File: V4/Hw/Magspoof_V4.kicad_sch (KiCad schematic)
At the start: 35 parts, among them J1 Coil, J2 SWD, P1 USB_C_Plug_USB2.0, Q1 DMG3415U-7, SW1 ON, SW3 S1, SW4 SOURCE MAG, SW5 RESET, U1 CH552G, U2 AP2112K-3.3, U3 TC4424, U5 MCP73831

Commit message: add lcsc components to BOM
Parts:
- C1, C2: LCSC# (none) -> C2171572; Proveedor MOUSER -> LCSC
- C17, C18, C3, C4: LCSC# C2992625 -> C315248; manf# 0402X106M100CT -> CL05A106MP5NUNC
- D3: LCSC# (none) -> C205442; Proveedor MOUSER -> LCSC
- D4: LCSC# (none) -> C130114
- F1: LCSC# (none) -> C2649565
- R1: LCSC# (none) -> C2759509
- R10: LCSC# (none) -> C114877
- R11: LCSC# (none) -> C192169
- R7: LCSC# (none) -> C138045
- SW1: LCSC# - -> C221660; Proveedor (none) -> LCSC
- SW4: LCSC# (none) -> C221660; Proveedor MOUSER -> LCSC
- U3: LCSC# (none) -> C636876; Proveedor (none) -> MOUSER
- U5: LCSC# (none) -> C38066
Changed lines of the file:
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@@
       (effects (font (size 1.27 1.27)) hide)
     )
-    (property "LCSC#" "" (at 216.789 77.216 0)
+    (property "LCSC#" "C636876" (at 216.789 77.216 0)
+      (effects (font (size 1.27 1.27)) hide)
+    )
+    (property "Proveedor" "MOUSER" (at 216.789 77.216 0)
       (effects (font (size 1.27 1.27)) hide)
     )
@@
       (effects (font (size 1.27 1.27)) hide)
     )
+    (property "LCSC#" "C38066" (at 228.854 27.686 0)
+      (effects (font (size 1.27 1.27)) hide)
+    )
     (pin "1")
     (pin "2")
@@
       (effects (font (size 1.27 1.27)) hide)
     )
-    (property "manf#" "0402X106M100CT" (at 118.872 39.497 0)
-      (effects (font (size 1.27 1.27)) hide)
-    )
-    (property "LCSC#" "C2992625" (at 118.872 39.497 0)
+    (property "manf#" "CL05A106MP5NUNC" (at 118.872 39.497 0)
+      (effects (font (size 1.27 1.27)) hide)
+    )
+    (property "LCSC#" "C315248" (at 118.872 39.497 0)
       (effects (font (size 1.27 1.27)) hide)
     )
@@
       (effects (font (size 1.27 1.27)) hide)
     )
-    (property "LCSC#" "" (at 107.061 107.442 0)
+    (property "LCSC#" "C2759509" (at 107.061 107.442 0)
       (effects (font (size 1.27 1.27)) hide)
     )
@@
       (effects (font (size 1.27 1.27)) hide)
     )
-    (property "LCSC#" "" (at 147.32 43.053 0)
+    (property "LCSC#" "C138045" (at 147.32 43.053 0)
       (effects (font (size 1.27 1.27)) hide)
     )
@@
       (effects (font (size 1.27 1.27)) hide)
     )
-    (property "LCSC#" "" (at 53.34 106.68 0)
-      (effects (font (size 1.27 1.27)) hide)
-    )
-    (property "Proveedor" "MOUSER" (at 53.34 106.68 0)
+    (property "LCSC#" "C2171572" (at 53.34 106.68 0)
+      (effects (font (size 1.27 1.27)) hide)
+    )
+    (property "Proveedor" "LCSC" (at 53.34 106.68 0)
       (effects (font (size 1.27 1.27)) hide)
     )
@@
       (effects (font (size 1.27 1.27)) hide)
     )
-    (property "manf#" "0402X106M100CT" (at 201.295 36.576 0)
-      (effects (font (size 1.27 1.27)) hide)
-    )
-    (property "LCSC#" "C2992625" (at 201.295 36.576 0)
+    (property "manf#" "CL05A106MP5NUNC" (at 201.295 36.576 0)
+      (effects (font (size 1.27 1.27)) hide)
+    )
+    (property "LCSC#" "C315248" (at 201.295 36.576 0)
       (effects (font (size 1.27 1.27)) hide)
     )
@@
       (effects (font (size 1.27 1.27)) hide)
     )
+    (property "LCSC#" "C114877" (at 243.713 35.687 0)
+      (effects (font (size 1.27 1.27)) hide)
+    )
     (pin "1")
     (pin "2")
@@
       (effects (font (size 1.27 1.27)) hide)
     )
-    (property "LCSC#" "-" (at 85.725 36.957 0)
+    (property "LCSC#" "C221660" (at 85.725 36.957 0)
       (effects (font (size 1.27 1.27)) hide)
     )
     (property "manf#" "JS102011SAQN" (at 85.725 36.957 0)
+      (effects (font (size 1.27 1.27)) hide)
+    )
+    (property "Proveedor" "LCSC" (at 85.725 36.957 0)
       (effects (font (size 1.27 1.27)) hide)
     )
@@
       (effects (font (size 1.27 1.27)) hide)
     )
+    (property "LCSC#" "C130114" (at 243.713 44.45 0)
+      (effects (font (size 1.27 1.27)) hide)
+    )
     (pin "1")
     (pin "2")
@@
       (effects (font (size 1.27 1.27)) hide)
     )
-    (property "Proveedor" "MOUSER" (at 147.32 32.512 0)
+    (property "Proveedor" "LCSC" (at 147.32 32.512 0)
+      (effects (font (size 1.27 1.27)) hide)
+    )
+    (property "LCSC#" "C205442" (at 147.32 32.512 0)
       (effects (font (size 1.27 1.27)) hide)
     )
@@
       (effects (font (size 1.27 1.27)) hide)
     )
-    (property "manf#" "0402X106M100CT" (at 94.488 41.529 0)
-      (effects (font (size 1.27 1.27)) hide)
-    )
-    (property "LCSC#" "C2992625" (at 94.488 41.529 0)
+    (property "manf#" "CL05A106MP5NUNC" (at 94.488 41.529 0)
+      (effects (font (size 1.27 1.27)) hide)
+    )
+    (property "LCSC#" "C315248" (at 94.488 41.529 0)
       (effects (font (size 1.27 1.27)) hide)
     )
@@
       (effects (font (size 1.27 1.27)) hide)
     )
-    (property "LCSC#" "" (at 65.532 43.688 0)
+    (property "LCSC#" "C192169" (at 65.532 43.688 0)
       (effects (font (size 1.27 1.27)) hide)
     )
@@
       (effects (font (size 1.27 1.27)) hide)
     )
-    (property "manf#" "0402X106M100CT" (at 262.001 36.703 0)
-      (effects (font (size 1.27 1.27)) hide)
-    )
-    (property "LCSC#" "C2992625" (at 262.001 36.703 0)
+    (property "manf#" "CL05A106MP5NUNC" (at 262.001 36.703 0)
+      (effects (font (size 1.27 1.27)) hide)
+    )
+    (property "LCSC#" "C315248" (at 262.001 36.703 0)
       (effects (font (size 1.27 1.27)) hide)
     )
@@
       (effects (font (size 1.27 1.27)) hide)
     )
-    (property "Proveedor" "MOUSER" (at 239.649 73.406 0)
+    (property "Proveedor" "LCSC" (at 239.649 73.406 0)
+      (effects (font (size 1.27 1.27)) hide)
+    )
+    (property "LCSC#" "C221660" (at 239.649 73.406 0)
       (effects (font (size 1.27 1.27)) hide)
     )
@@
       (effects (font (size 1.27 1.27)) hide)
     )
-    (property "LCSC#" "" (at 58.801 100.33 0)
-      (effects (font (size 1.27 1.27)) hide)
-    )
-    (property "Proveedor" "MOUSER" (at 58.801 100.33 0)
+    (property "LCSC#" "C2171572" (at 58.801 100.33 0)
+      (effects (font (size 1.27 1.27)) hide)
+    )
+    (property "Proveedor" "LCSC" (at 58.801 100.33 0)
       (effects (font (size 1.27 1.27)) hide)
     )
@@
       (effects (font (size 1.27 1.27)) hide)
     )
+    (property "LCSC#" "C2649565" (at 45.339 30.48 0)
+      (effects (font (size 1.27 1.27)) hide)
+    )

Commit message: Change components for JLCPCB
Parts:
- F1: footprint Fuse:Fuse_0805_2012Metric -> Fuse:Fuse_0603_1608Metric; LCSC# C2649565 -> C136327; Proveedor MOUSER -> LCSC; manf# MFU0805FF00500P100 -> (none)
- SW1, SW4: footprint Library:JS102011SAQN -> Library:SW-SMD_K3-1280S-K1; LCSC# C221660 -> C92658; manf# JS102011SAQN -> (none)
- U3: LCSC# C636876 -> C44150; manf# TC4424AVOA -> TC4424AVOA713
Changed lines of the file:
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@@
       (effects (font (size 1.524 1.524)) hide)
     )
-    (property "manf#" "TC4424AVOA" (at 216.789 77.216 0)
-      (effects (font (size 1.27 1.27)) hide)
-    )
-    (property "LCSC#" "C636876" (at 216.789 77.216 0)
+    (property "manf#" "TC4424AVOA713" (at 216.789 77.216 0)
+      (effects (font (size 1.27 1.27)) hide)
+    )
+    (property "LCSC#" "C44150" (at 216.789 77.216 0)
       (effects (font (size 1.27 1.27)) hide)
     )
@@
       (effects (font (size 1.27 1.27)))
     )
-    (property "Footprint" "Library:JS102011SAQN" (at 85.725 36.957 0)
+    (property "Footprint" "Library:SW-SMD_K3-1280S-K1" (at 85.725 36.957 0)
       (effects (font (size 1.27 1.27)) hide)
     )
@@
       (effects (font (size 1.27 1.27)) hide)
     )
-    (property "LCSC#" "C221660" (at 85.725 36.957 0)
-      (effects (font (size 1.27 1.27)) hide)
-    )
-    (property "manf#" "JS102011SAQN" (at 85.725 36.957 0)
+    (property "LCSC#" "C92658" (at 85.725 36.957 0)
+      (effects (font (size 1.27 1.27)) hide)
+    )
+    (property "manf#" "" (at 85.725 36.957 0)
       (effects (font (size 1.27 1.27)) hide)
     )
@@
       (effects (font (size 1.27 1.27)) (justify left))
     )
-    (property "Footprint" "Library:JS102011SAQN" (at 239.649 73.406 0)
+    (property "Footprint" "Library:SW-SMD_K3-1280S-K1" (at 239.649 73.406 0)
       (effects (font (size 1.27 1.27)) hide)
     )
@@
       (effects (font (size 1.27 1.27)) hide)
     )
-    (property "manf#" "JS102011SAQN" (at 239.649 73.406 0)
+    (property "manf#" "" (at 239.649 73.406 0)
       (effects (font (size 1.27 1.27)) hide)
     )
@@
       (effects (font (size 1.27 1.27)) hide)
     )
-    (property "LCSC#" "C221660" (at 239.649 73.406 0)
+    (property "LCSC#" "C92658" (at 239.649 73.406 0)
+      (effects (font (size 1.27 1.27)) hide)
+    )
+    (property "Campo7" "" (at 239.649 73.406 90)
       (effects (font (size 1.27 1.27)) hide)
     )
@@
       (effects (font (size 1.27 1.27)))
     )
-    (property "Footprint" "Fuse:Fuse_0805_2012Metric" (at 45.339 30.48 0)
+    (property "Footprint" "Fuse:Fuse_0603_1608Metric" (at 45.339 30.48 0)
       (effects (font (size 1.27 1.27)) hide)
     )
@@
       (effects (font (size 1.27 1.27)) hide)
     )
-    (property "manf#" "MFU0805FF00500P100" (at 45.339 30.48 0)
-      (effects (font (size 1.27 1.27)) hide)
-    )
-    (property "Proveedor" "MOUSER" (at 45.339 30.48 0)
-      (effects (font (size 1.27 1.27)) hide)
-    )
-    (property "LCSC#" "C2649565" (at 45.339 30.48 0)
-      (effects (font (size 1.27 1.27)) hide)
-    )
+    (property "manf#" "" (at 45.339 30.48 0)
+      (effects (font (size 1.27 1.27)) hide)
+    )
+    (property "Proveedor" "LCSC" (at 45.339 30.48 0)
+      (effects (font (size 1.27 1.27)) hide)
+    )
+    (property "LCSC#" "C136327" (at 45.339 30.48 0)
+      (effects (font (size 1.27 1.27)) hide)
+    )

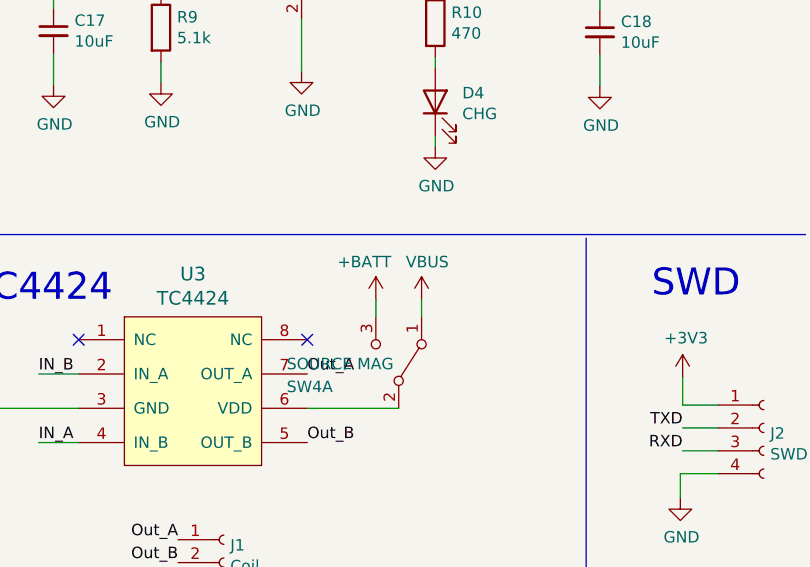
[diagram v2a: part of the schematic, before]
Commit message: change footprint of SW1,4, and F1 and routing
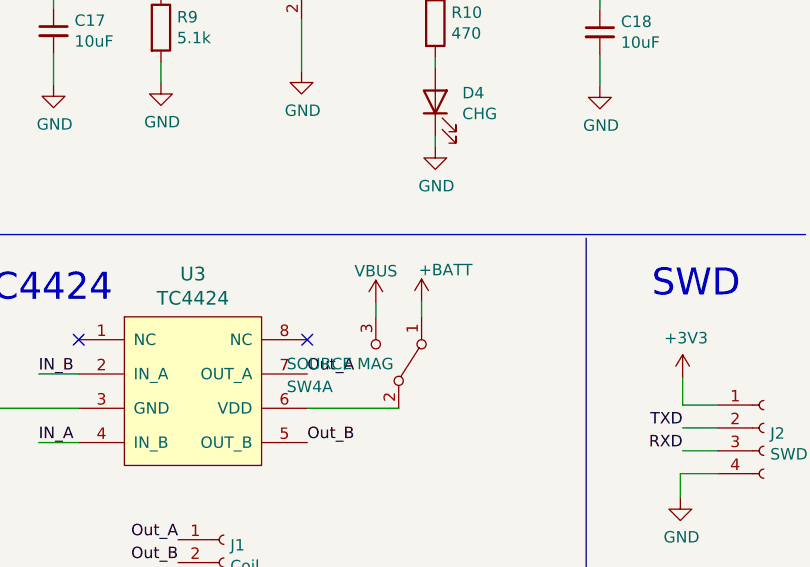
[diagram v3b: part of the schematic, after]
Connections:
- net +BATT: now also SW4.1 (A); no longer SW4.3 (C)
- net VBUS: now also SW4.3 (C); no longer SW4.1 (A)
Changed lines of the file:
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@@
-    (stroke (width 0) (type default))
-  )
-  (wire (pts (xy 237.109 68.326) (xy 237.109 66.421))
     (stroke (width 0) (type default))
   )
@@
     (stroke (width 0) (type default))
   )
+  (wire (pts (xy 242.189 66.675) (xy 242.189 68.326))
+    (stroke (width 0) (type default))
+  )
   (wire (pts (xy 79.121 105.41) (xy 82.169 105.41))
     (stroke (width 0) (type default))
@@
     (stroke (width 0) (type default))
   )
+  (wire (pts (xy 237.109 66.802) (xy 237.109 68.326))
+    (stroke (width 0) (type default))
+  )
   (wire (pts (xy 40.386 35.56) (xy 41.783 35.56))
     (stroke (width 0) (type default))
   )
   (wire (pts (xy 94.488 38.989) (xy 94.488 36.957))
-    (stroke (width 0) (type default))
-  )
-  (wire (pts (xy 242.189 68.326) (xy 242.189 66.421))
     (stroke (width 0) (type default))
   )
@@
     )
   )
-  (symbol (lib_id "power:+BATT") (at 237.109 66.421 0) (unit 1)
-    (in_bom yes) (on_board yes) (dnp no)
-    (property "Reference" "#PWR057" (at 237.109 70.231 0)
-      (effects (font (size 1.27 1.27)) hide)
-    )
-    (property "Value" "+BATT" (at 235.839 62.23 0)
-      (effects (font (size 1.27 1.27)))
-    )
-    (property "Footprint" "" (at 237.109 66.421 0)
-      (effects (font (size 1.27 1.27)) hide)
-    )
-    (property "Datasheet" "" (at 237.109 66.421 0)
+  (symbol (lib_id "power:+BATT") (at 242.189 66.675 0) (unit 1)
+    (in_bom yes) (on_board yes) (dnp no)
+    (property "Reference" "#PWR057" (at 242.189 70.485 0)
+      (effects (font (size 1.27 1.27)) hide)
+    )
+    (property "Value" "+BATT" (at 244.856 63.119 0)
+      (effects (font (size 1.27 1.27)))
+    )
+    (property "Footprint" "" (at 242.189 66.675 0)
+      (effects (font (size 1.27 1.27)) hide)
+    )
+    (property "Datasheet" "" (at 242.189 66.675 0)
       (effects (font (size 1.27 1.27)) hide)
     )
@@
     )
   )
-  (symbol (lib_id "power:VBUS") (at 242.189 66.421 0) (unit 1)
-    (in_bom yes) (on_board yes) (dnp no)
-    (property "Reference" "#PWR058" (at 242.189 70.231 0)
-      (effects (font (size 1.27 1.27)) hide)
-    )
-    (property "Value" "VBUS" (at 242.824 62.23 0)
-      (effects (font (size 1.27 1.27)))
-    )
-    (property "Footprint" "" (at 242.189 66.421 0)
-      (effects (font (size 1.27 1.27)) hide)
-    )
-    (property "Datasheet" "" (at 242.189 66.421 0)
-      (effects (font (size 1.27 1.27)) hide)
-    )
+  (symbol (lib_id "power:VBUS") (at 237.109 66.802 0) (unit 1)
+    (in_bom yes) (on_board yes) (dnp no)
+    (property "Reference" "#PWR058" (at 237.109 70.612 0)
+      (effects (font (size 1.27 1.27)) hide)
+    )
+    (property "Value" "VBUS" (at 237.109 63.246 0)
+      (effects (font (size 1.27 1.27)))
+    )
+    (property "Footprint" "" (at 237.109 66.802 0)
+      (effects (font (size 1.27 1.27)) hide)
+    )
+    (property "Datasheet" "" (at 237.109 66.802 0)
+      (effects (font (size 1.27 1.27)) hide)
+    )

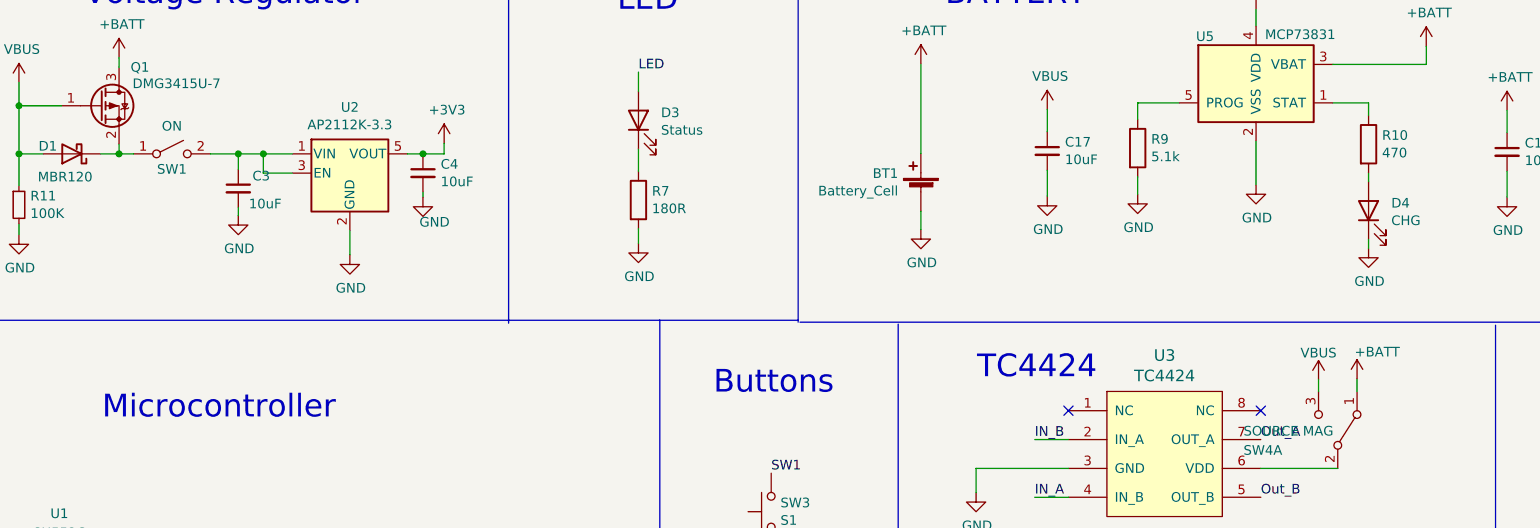
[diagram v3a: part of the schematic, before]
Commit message: change SW1 and SW4 for stocks
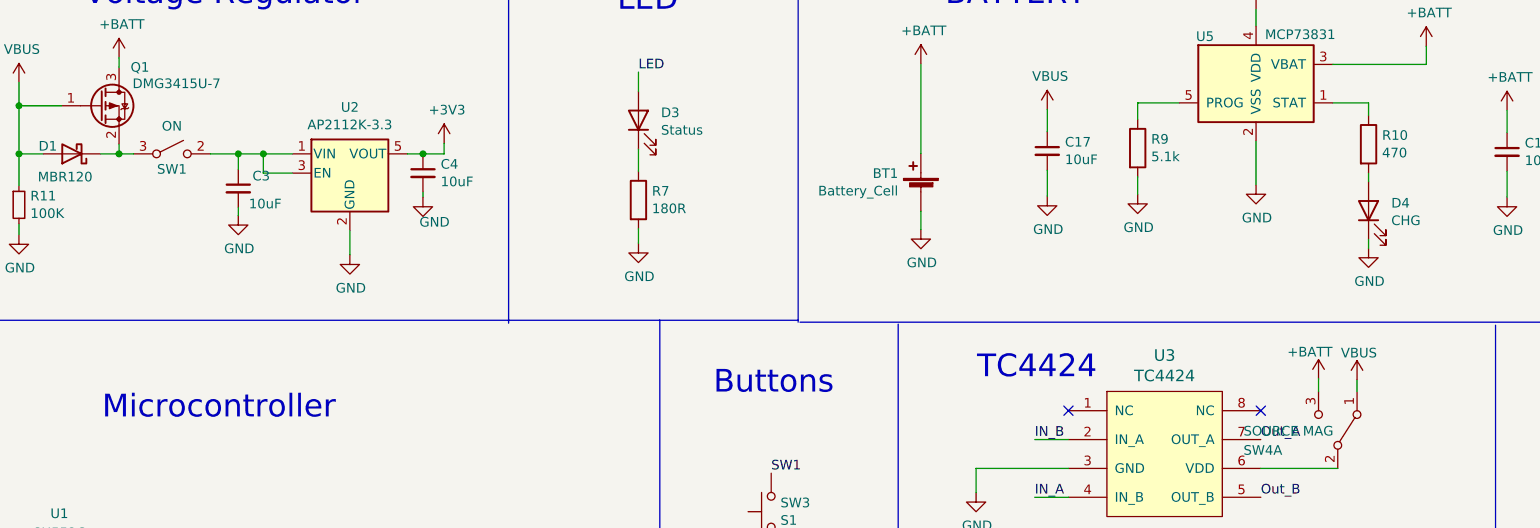
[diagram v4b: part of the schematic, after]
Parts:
- SW1, SW4: footprint Library:SW-SMD_K3-1280S-K1 -> Library:SW-SMD_SSSS811101; LCSC# C92658 -> C109335
- SW3, SW5: LCSC# C2886897 -> C318889
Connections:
- net +BATT: now also SW4.3 (C); no longer SW4.1 (A)
- net VBUS: now also SW4.1 (A); no longer SW4.3 (C)
- net at D1.1 (K), Q1.2 (S): now also SW1.3 (A); no longer SW1.1 (A)
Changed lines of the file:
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@@
-    (stroke (width 0) (type default))
-  )
-  (wire (pts (xy 242.189 66.675) (xy 242.189 68.326))
     (stroke (width 0) (type default))
   )
@@
     (stroke (width 0) (type default))
   )
+  (wire (pts (xy 237.109 66.675) (xy 237.109 68.326))
+    (stroke (width 0) (type default))
+  )
   (wire (pts (xy 271.1958 78.1304) (xy 271.1958 75.0824))
     (stroke (width 0) (type default))
@@
     (stroke (width 0) (type default))
   )
-  (wire (pts (xy 237.109 66.802) (xy 237.109 68.326))
-    (stroke (width 0) (type default))
-  )
   (wire (pts (xy 40.386 35.56) (xy 41.783 35.56))
     (stroke (width 0) (type default))
@@
   )
   (wire (pts (xy 110.744 96.647) (xy 108.204 96.647))
+    (stroke (width 0) (type default))
+  )
+  (wire (pts (xy 242.189 66.802) (xy 242.189 68.326))
     (stroke (width 0) (type default))
   )
@@
     )
   )
-  (symbol (lib_id "power:+BATT") (at 242.189 66.675 0) (unit 1)
-    (in_bom yes) (on_board yes) (dnp no)
-    (property "Reference" "#PWR057" (at 242.189 70.485 0)
-      (effects (font (size 1.27 1.27)) hide)
-    )
-    (property "Value" "+BATT" (at 244.856 63.119 0)
-      (effects (font (size 1.27 1.27)))
-    )
-    (property "Footprint" "" (at 242.189 66.675 0)
-      (effects (font (size 1.27 1.27)) hide)
-    )
-    (property "Datasheet" "" (at 242.189 66.675 0)
+  (symbol (lib_id "power:+BATT") (at 237.109 66.675 0) (unit 1)
+    (in_bom yes) (on_board yes) (dnp no)
+    (property "Reference" "#PWR057" (at 237.109 70.485 0)
+      (effects (font (size 1.27 1.27)) hide)
+    )
+    (property "Value" "+BATT" (at 235.966 63.119 0)
+      (effects (font (size 1.27 1.27)))
+    )
+    (property "Footprint" "" (at 237.109 66.675 0)
+      (effects (font (size 1.27 1.27)) hide)
+    )
+    (property "Datasheet" "" (at 237.109 66.675 0)
       (effects (font (size 1.27 1.27)) hide)
     )
@@
       (effects (font (size 1.27 1.27)) hide)
     )
-    (property "LCSC#" "C2886897" (at 164.846 84.201 0)
+    (property "LCSC#" "C318889" (at 164.846 84.201 0)
       (effects (font (size 1.27 1.27)) hide)
     )
@@
       (effects (font (size 1.27 1.27)))
     )
-    (property "Footprint" "Library:SW-SMD_K3-1280S-K1" (at 85.725 36.957 0)
+    (property "Footprint" "Library:SW-SMD_SSSS811101" (at 85.725 36.957 0)
       (effects (font (size 1.27 1.27)) hide)
     )
@@
       (effects (font (size 1.27 1.27)) hide)
     )
-    (property "LCSC#" "C92658" (at 85.725 36.957 0)
+    (property "LCSC#" "C109335" (at 85.725 36.957 0)
       (effects (font (size 1.27 1.27)) hide)
     )
@@
       (effects (font (size 1.27 1.27)) hide)
     )
-    (pin "1")
+    (pin "3")
     (pin "2")
     (instances
@@
     )
   )
-  (symbol (lib_id "power:VBUS") (at 237.109 66.802 0) (unit 1)
-    (in_bom yes) (on_board yes) (dnp no)
-    (property "Reference" "#PWR058" (at 237.109 70.612 0)
-      (effects (font (size 1.27 1.27)) hide)
-    )
-    (property "Value" "VBUS" (at 237.109 63.246 0)
-      (effects (font (size 1.27 1.27)))
-    )
-    (property "Footprint" "" (at 237.109 66.802 0)
-      (effects (font (size 1.27 1.27)) hide)
-    )
-    (property "Datasheet" "" (at 237.109 66.802 0)
+  (symbol (lib_id "power:VBUS") (at 242.189 66.802 0) (unit 1)
+    (in_bom yes) (on_board yes) (dnp no)
+    (property "Reference" "#PWR058" (at 242.189 70.612 0)
+      (effects (font (size 1.27 1.27)) hide)
+    )
+    (property "Value" "VBUS" (at 242.443 63.246 0)
+      (effects (font (size 1.27 1.27)))
+    )
+    (property "Footprint" "" (at 242.189 66.802 0)
+      (effects (font (size 1.27 1.27)) hide)
+    )
+    (property "Datasheet" "" (at 242.189 66.802 0)
       (effects (font (size 1.27 1.27)) hide)
     )
@@
       (effects (font (size 1.27 1.27)) (justify left))
     )
-    (property "Footprint" "Library:SW-SMD_K3-1280S-K1" (at 239.649 73.406 0)
+    (property "Footprint" "Library:SW-SMD_SSSS811101" (at 239.649 73.406 0)
       (effects (font (size 1.27 1.27)) hide)
     )
@@
       (effects (font (size 1.27 1.27)) hide)
     )
-    (property "LCSC#" "C92658" (at 239.649 73.406 0)
+    (property "LCSC#" "C109335" (at 239.649 73.406 0)
       (effects (font (size 1.27 1.27)) hide)
     )
@@
       (effects (font (size 1.27 1.27)) hide)
     )
-    (property "LCSC#" "C2886897" (at 115.824 96.647 0)
-      (effects (font (size 1.27 1.27)) hide)
-    )
+    (property "LCSC#" "C318889" (at 115.824 96.647 0)
+      (effects (font (size 1.27 1.27)) hide)
+    )
